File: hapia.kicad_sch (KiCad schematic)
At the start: 192 parts, among them J1 Micro_SD_Card, J10 USB_C_Receptacle_USB2.0_16P, J11 USB_A, J12 Micro_SD_Card, J2 SUB_placa_de_controle, J3 Conn_01x15_Pin, J4 ATX-20, J5 Conn_01x10, J6 Conn_01x04_Pin, J7 Conn_01x04_Pin, J8 Conn_01x04_Pin, J9 Conn_01x04_Pin, M1 Fan, M2 Fan, M3 Fan, Q1 NMOS, Q2 NMOS, Q3 NMOS, Q4 NMOS, SW1 SW_Push, SW2 SW_Push, U1 SRV05-4, U10 SRV05-4, U2 STM32F407VETx, U3 TMC2209-LA, U4 TMC2209-LA, U5 TPS54302, U6 TMC2209-LA, U7 TMC2209-LA, U8 MIC4427, U9 MIC4427, Y1 Crystal

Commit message: revisão 29072026 kicad 10
mais robusta, completa e mais perto de um lançamento funcional
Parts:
- removed C15, C18, C20, C21, C27, C31, C32, C33, C34, C36, C39, C40, C41, C46, C52, C58, C59, C61, C62, C64, C66, C71, C72, C74, C78, C79: 100nf, symbol Device:C
- removed C19, C35, C38, C63, C65: 1uf, symbol Device:C
- removed C23: 470µf, symbol Device:C_Polarized
- removed C26, C45, C47, C49, C73, C75: 10uf, symbol Device:C
- removed C28, C30, C56, C57: 22nf, symbol Device:C
- removed C29, C37, C43, C67, C69: 10nf, symbol Device:C
- removed C42, C44, C70: 4.7uf, symbol Device:C
- removed C48, C50, C76, C77: 100uf, symbol Device:C
- removed C51: 470uf, symbol Device:C
- removed C54: 100µf, symbol Device:C_Polarized
- removed C60: 1nf, symbol Device:C
- removed D1: SMF15A, Diode_SMD:D_SMF, symbol Diode:SMF15A
- removed D2: SMF33A, Diode_SMD:D_SMF, symbol Diode:SMF33A
- removed F1, F3, F4: Polyfuse, symbol Device:Polyfuse
- removed F2, F5: Fuse, symbol Device:Fuse
- removed FB1: FerriteBead, symbol Device:FerriteBead
- removed J1, J12: Micro_SD_Card, symbol Connector:Micro_SD_Card
- removed J11: USB_A, Connector_USB:USB_A_Molex_67643_Horizontal, symbol Connector:USB_A
- removed J2: SUB_placa_de_controle, Connector_PinHeader_2.54mm:PinHeader_1x10_P2.54mm_Vertical, symbol Connector_Generic:Conn_01x10
- removed J3: Conn_01x15_Pin, Connector_PinSocket_2.54mm:PinSocket_1x15_P2.54mm_Vertical, symbol Connector:Conn_01x15_Pin
- removed J4: ATX-20, Connector_Molex:Molex_Mini-Fit_Jr_5566-20A_2x10_P4.20mm_Vertical, symbol Connector:ATX-20
- removed J5: Conn_01x10, symbol Connector_Generic:Conn_01x10
- removed J6, J7, J8, J9: Conn_01x04_Pin, Connector_JST:JST_EH_B4B-EH-A_1x04_P2.50mm_Vertical, symbol Connector:Conn_01x04_Pin
- removed L1: 6.8uh, Inductor_SMD:L_Bourns_SRP1038C_10.0x10.0mm, symbol Device:L
- removed M1, M2, M3: Fan, symbol Motor:Fan
- removed Q1, Q2, Q3, Q4: NMOS, symbol Simulation_SPICE:NMOS
- removed R22, R23, R24, R25, R26, R27, R28, R29, R37, R38, R39, R40, R76, R77: 33r, symbol Device:R
- removed R34, R35, R36: 1k, symbol Device:R
- removed R41, R42, R43, R44, R53, R55, R56, R57, R58: 100k, symbol Device:R
- removed R45, R46, R59, R60: 20k, symbol Device:R
- removed R47, R48, R49, R50, R61, R62, R63, R64: 11r, symbol Device:R
- removed R51, R52: 10kΩ, symbol Device:R
- removed R54: 22k, symbol Device:R
- removed R65: 1Ωm, symbol Device:R
- removed R66, R67, R68, R73: 10k, symbol Device:R
- removed R69, R70: exrtusora, symbol Device:Heater
- removed R74: R, symbol Device:R
- removed TH1, TH2: 10k, symbol Device:Thermistor_NTC
- removed TP1, TP2, TP3, TP4, TP6, TP7, TP8, TP9: TestPoint, Connector_USB:USB_Micro-B_Amphenol_10104110_Horizontal, symbol Connector:TestPoint
- removed U1: SRV05-4, Package_TO_SOT_SMD:SOT-23-6, symbol Power_Protection:SRV05-4
- removed U3, U4, U6, U7: TMC2209-LA, Package_DFN_QFN:VQFN-28-1EP_5x5mm_P0.5mm_EP3.7x3.7mm_ThermalVias, symbol Driver_Motor:TMC2209-LA
- removed U5: TPS54302, Package_TO_SOT_SMD:SOT-23-6, symbol Regulator_Switching:TPS54302
- removed U8, U9: MIC4427, symbol Driver_FET:MIC4427
- added C14: 10µf, symbol Device:C
- added C95: 1µf, symbol Device:C
- added D5: SMF33A, Diode_SMD:D_SMF, symbol Diode:SMF33A
- added JP1: usb/atx, symbol Jumper:SolderJumper_3_Bridged12
- added R10, R16, R6, R7, R8, R9: 33Ω, symbol Device:R
- added R18: 10kΩ, symbol Device:R
- added unit 8 of RN1
- added unit 3 of RN3
- added unit 2 of RN3
- added unit 5 of RN3
- added unit 7 of RN3
- added unit 6 of RN3
- added unit 1 of RN3
- added unit 4 of RN3
- added RN4, RN5: 33Ω, Resistor_SMD:R_Array_Convex_4x0603, symbol Device:R_Pack04_Split
- added TP16: 3.3va, TestPoint:TestPoint_Pad_D1.0mm, symbol Connector:TestPoint
- added U1: AMS1117-3.3, Package_TO_SOT_SMD:SOT-223-3_TabPin2, symbol Regulator_Linear:AMS1117-3.3
- C1: value pf -> 22pf; footprint (none) -> Capacitor_SMD:C_0603_1608Metric_Pad1.08x0.95mm_HandSolder; jlc_pcb: (none) -> C561800; mpn (none) -> C0603C220J4GAC7867
- C10, C2, C3, C4, C5, C6, C7, C9: footprint (none) -> Capacitor_SMD:C_0603_1608Metric; jlc_pcb/lcsc_ID: (none) -> C346191; jlc_pcb: (none) -> C346191; mpn (none) -> CL10B104KB8NFNC
- C11: renamed from C13; value pf -> 22pf; footprint (none) -> Capacitor_SMD:C_0603_1608Metric_Pad1.08x0.95mm_HandSolder; jlc_pcb: (none) -> C561800; mpn (none) -> C0603C220J4GAC7867
- C12: renamed from C11; footprint (none) -> Capacitor_SMD:C_0603_1608Metric; jlc_pcb/lcsc_ID: (none) -> C346191; jlc_pcb: (none) -> C346191; mpn (none) -> CL10B104KB8NFNC
- C13: renamed from C12; value 10uf -> 10µf
- C15: renamed from C14; value 4.7uf -> 2.2µf
- C16: value 10uf -> 2.2µf
- C17: value 4.7uf -> 1µf
- C68: value 4.7uf -> 100nf; footprint (none) -> Capacitor_SMD:C_0603_1608Metric; jlc_pcb/lcsc_ID: (none) -> C346191; jlc_pcb: (none) -> C346191; mpn (none) -> CL10B104KB8NFNC
- C8: value 10uf -> 100nf; footprint (none) -> Capacitor_SMD:C_0603_1608Metric; jlc_pcb/lcsc_ID: (none) -> C346191; jlc_pcb: (none) -> C346191; mpn (none) -> CL10B104KB8NFNC
- R1, R2: value 10K -> 10KΩ
- R19: renamed from R75; value R -> 10kΩ
- R20: renamed from R71; value 5.1Ωk -> 5.1kΩ
- R21: renamed from R72; value 5.1Ωk -> 5.1kΩ
- R3, R4: value 4.7k -> 33Ω
- R5: value 33r -> 33Ω
- TP1: renamed from TP5; value TestPoint -> 3.3v; footprint Connector_USB:USB_Micro-B_Amphenol_10104110_Horizontal -> TestPoint:TestPoint_Pad_D1.0mm
- TP2: renamed from TP10; footprint Connector_USB:USB_Micro-B_Amphenol_10104110_Horizontal -> TestPoint:TestPoint_Pad_D1.0mm
- U2: value STM32F407VETx -> STM32F407VET6; jlc_pcb: (none) -> C28730; mpn (none) -> STM32F407VET6
- U3: renamed from U10; jlc_pcb: (none) -> ssss; mpn (none) -> ssss
- Y1: value Crystal -> 8mhz; footprint (none) -> Crystal:Crystal_SMD_5032-2Pin_5.0x3.2mm_HandSoldering; jlc_pcb: (none) -> C144380; mpn (none) -> ABM3-8.000MHZ-D2Y-T
- renumbered J10 to J1, R78 to R11, R30 to R12, R31 to R13, R32 to R14, R33 to R15, RN1 to RN2, RN2 to RN3
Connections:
- net PGND is gone; now on an unnamed net: C68.1
- net TMC_4vut is gone; now on net GND: C68.2
- net USB_D+ is gone; now on net USB_C_D+: RN3.9 (R8.2)
- net USB_D- is gone; now on net USB_C_D-: RN2.10 (R7.2)
- net +3.3V: now also JP1.3 (B); no longer C10.1, C12.1, C13.1, C16.1, C2.1, C3.1, C4.1, C5.1, C6.1, C7.1, C8.1, C9.1, FB2.2, R1.2, R2.2, R3.1, R4.1, SW1.2, SW2.2, U2.100 (VDD), U2.11 (VDD), U2.14 (NRST), U2.19 (VDD), U2.28 (VDD), U2.50 (VDD), U2.6 (VBAT), U2.75 (VDD), U2.94 (BOOT0)
- net Fan_1: now also R8.2
- net Fan_2: now also R4.2; no longer R5.2
- net GND: now also C14.2, C95.2, D5.2 (A2), U1.1 (GND)
- net SUB_2: now also RN3.14 (R3.2); no longer U2.91 (PB5)
- net SUB_3: now also RN3.13 (R4.2); no longer U2.92 (PB6)
- net SUB_4: now also RN3.12 (R5.2); no longer U2.93 (PB7)
- net SUB_5: now also RN3.11 (R6.2); no longer U2.95 (PB8)
- net SUB_6: now also RN3.10 (R7.2); no longer U2.96 (PB9)
- net SUB_SCL: now also RN3.16 (R1.2); no longer R4.2
- net SUB_SDA: now also RN3.15 (R2.2); no longer R3.2
- net USB_det_2.5v: now also R18.2
- net exrtusora: now also R6.2
- net gpi_PD14: now also R10.2
- net gpi_PD15: now also R9.2
- net hot_bed: now also R7.2
- net sd_cs: now also R5.2
- net at U2.25 (PA2): now also RN4.8 (R1.2)
- net at U2.26 (PA3): now also RN4.7 (R2.2)
- net at U2.36 (PB1): now also R7.1
- net at U2.35 (PB0): now also R6.1
- net at U2.73 (VCAP_2): now also C16.1; no longer C17.1
- net at R15.2, U2.24 (PA1): now also R16.1
- net at U2.22 (VDDA): now also FB2.1, C95.1, TP16.1; no longer TP1.1
- net at U2.29 (PA4): now also RN4.6 (R3.2)
- net at U2.30 (PA5): now also RN4.5 (R4.2)
- net at U2.31 (PA6): now also RN5.8 (R1.2)
- net at U2.32 (PA7): now also RN5.7 (R2.2)
- net at U2.33 (PC4): now also RN5.6 (R3.2)
- net at U2.34 (PC5): now also RN5.5 (R4.2)
- net at U2.37 (PB2): now also R8.1
- net at U2.38 (PE7): now also R4.1; no longer R5.1
- net NTC_MUX_out: now reaches U2.39 (PE8)
- net NTC_MUX_0: now reaches U2.40 (PE9)
- net NTC_MUX_1: now reaches U2.41 (PE10)
- net NTC_MUX_2: now reaches U2.42 (PE11)
- net at U2.63 (PC6): now also R9.1
- net at U2.64 (PC7): now also R10.1
- net at U2.77 (PA15): now also R5.1
- net at U2.89 (PB3): now also RN3.1 (R1.1)
- net at U2.90 (PB4): now also RN3.2 (R2.1)
- net at U2.97 (PE0): now also RN1.8 (R8.1)
- net at U2.98 (PE1): now also R3.1
- net 3.3v/A: no longer names the net of U2.21 (VREF+)
- net USB_det renamed +5Vusb
- net +5Vusb: now also C14.1, R18.1, U1.3 (VI)
- new net: RN3.3 (R3.1), U2.91 (PB5)
- new net: RN3.5 (R5.1), U2.93 (PB7)
- new net: RN3.4 (R4.1), U2.92 (PB6)
- new net: RN3.6 (R6.1), U2.95 (PB8)
- new net: RN3.7 (R7.1), U2.96 (PB9)
- new net +3.3Vbus: C17.1, D5.1 (A1), JP1.1 (A), U1.2 (VO)
- new net 3.3v/1: C10.1, C12.1, C13.1, C2.1, C3.1, C4.1, C5.1, C6.1, C7.1, C8.1, C9.1, FB2.2, JP1.2 (C), R1.2, R2.2, SW1.2, SW2.2, TP1.1, U2.100 (VDD), U2.11 (VDD), U2.14 (NRST), U2.19 (VDD), U2.28 (VDD), U2.50 (VDD), U2.6 (VBAT), U2.75 (VDD), U2.94 (BOOT0)
- new net SUB_led: RN1.9 (R8.2)
- new net TMC_DIR_3: RN4.1 (R1.1), RN4.3 (R3.1), RN5.1 (R1.1), RN5.3 (R3.1)
- new net TMC_step_3: RN4.2 (R2.1), RN4.4 (R4.1), RN5.2 (R2.1), RN5.4 (R4.1)
- new net TMC_uart: R16.2
- new net cont_sd: R3.2
- no-connect marks 76 -> 36
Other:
- note added: "3.3vbus = usb 3.3v = atx"
- note added: "by todio"
- note added: "ele ja vem com alimentaçao por usb"
- moved on the sheet: C1, C10, C11, C12, C13, C15, C2, C3, C4, C5, C6, C7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

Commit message: 10082026/B
nova revisão
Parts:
- removed C10, C12, C6, C68, C7, C8, C9: 100nf, Capacitor_SMD:C_0603_1608Metric, symbol Device:C
- removed C15: 2.2µf, symbol Device:C
- removed C95: 1µf, symbol Device:C
- removed R1, R2: 10KΩ, symbol Device:R
- added C29: 4.7µf, symbol Device:C
- added CN1, CN2: C_Network04, Resistor_SMD:R_Array_Convex_4x0603, symbol Device:C_Network04
- added D1: RED, symbol Device:LED_Small
- added F1: Fuse, symbol Device:Fuse
- added J18: Conn_ARM_JTAG_SWD_10, symbol Connector:Conn_ARM_JTAG_SWD_10
- added R1: 470Ω, symbol Device:R_Small
- added R22, R23: 33Ω, symbol Device:R
- added R42, R43: 10KΩ, symbol Device:R
- added TP12: TestPoint, TestPoint:TestPoint_Pad_D1.0mm, symbol Connector:TestPoint
- C16: value 2.2µf -> 4.7µf
- TP16: value 3.3va -> TestPoint
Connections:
- net +5Vusb: now also F1.2; no longer J1.A4 (VBUS), J1.A9 (VBUS), J1.B4 (VBUS), J1.B9 (VBUS), TP2.1, U3.2 (VN)
- net 3.3v/1: now also CN1.1 (common), CN1.2 (C1), CN1.3 (C2), CN1.4 (C3), CN2.2 (C1), CN2.3 (C2), CN2.4 (C3), R42.2, R43.2; no longer C2.1, C3.1, C4.1, C5.1, SW1.2, SW2.2, U2.14 (NRST), U2.94 (BOOT0)
- net GND: now also C29.2, CN1.5 (C4), CN1.6 (C3), CN1.7 (C2), CN1.8 (C1), CN2.5 (C4), CN2.6 (C3), CN2.7 (C2), CN2.8 (C1), J18.3 (GND), J18.5 (GND), J18.9 (GNDDetect), R1.1
- net at RN3.2 (R2.1): no longer U2.90 (PB4)
- net VDDA: now reaches FB2.1, U2.22 (VDDA)
- net VDDA: now also U2.21 (VREF+), CN2.1 (common); no longer TP16.1
- net at U2.49 (VCAP_1): now also C4.1, C29.1
- net at U2.72 (PA13): now also R23.1
- net at C16.1, U2.73 (VCAP_2): now also C5.1
- net at U2.76 (PA14): now also R22.1
- net at RN3.1 (R1.1): no longer U2.89 (PB3)
- net +3.3Vbus renamed +3.3Vdev
- net +3.3Vdev: now also J18.1 (VTref)
- new net: D1.2 (A), F1.1, J1.A4 (VBUS), J1.A9 (VBUS), J1.B4 (VBUS), J1.B9 (VBUS), TP2.1, U3.2 (VN)
- new net: D1.1 (K), R1.2
- new net SDW_SWCLK: J18.4 (SWCLK/TCK), R22.2
- new net SDW_SWDIO: J18.2 (SWDIO/TMS), R23.2
- new net STM_boot: C3.1, R43.1, SW2.2, TP12.1, U2.94 (BOOT0)
- new net STM_nrst: C2.1, R42.1, SW1.2, TP16.1, U2.14 (NRST)
- new net SWD_SWO: J18.6 (SWO/TDO), U2.89 (PB3)
- new net SWD/jtag_rst: J18.10 (~{RESET}), U2.90 (PB4)
- no-connect marks 36 -> 34
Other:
- note added: "3.3vbus = usb, 3.3v = atx"
- note added: "Q1"
- note added: "Q1: o pino "shield" ta em "nc" por que essa impresora vai ser um "slave"/device, com modificação funciona com pendrive."
- note added: "Q2"
- note added: "se o mcu não tiver ligando com usb possivelmente o problema e o jumper(o pino do meio) não ligado a o pino de cima o 3.3vdev ou fusivel queimado. se esse não for o defeito provavelmente e algum componente com defeito."
- note removed: "3.3vbus = usb 3.3v = atx"
- company: (none) -> ---
- title: (none) -> hapia placa base.
- moved on the sheet: C13, FB2, R20, R21, RN3A, RN3B

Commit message: 10082026/D
"erros bobos"
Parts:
- CN1, CN2: value C_Network04 -> 100nf
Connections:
- net at RN3.2 (R2.1): now also U2.48 (PB11)
- net at U2.47 (PB10): now also RN3.1 (R1.1)
- no-connect marks 34 -> 33
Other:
- moved on the sheet: RN3A, RN3B
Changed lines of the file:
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@@
 	)
 	(no_connect
-		(at 128.27 163.83)
-	)
-	(no_connect
 		(at 201.93 66.04)
 	)
@@
 	)
 	(no_connect
-		(at 128.27 166.37)
+		(at 154.94 165.735)
 	)
 	(no_connect
@@
 	(global_label "SUB_SCL"
 		(shape input)
-		(at 160.655 146.05 0)
+		(at 135.89 163.83 0)
 		(fields_autoplaced yes)
 		(effects
@@
 		)
 		(property "Intersheetrefs" "${INTERSHEET_REFS}"
-			(at 171.9254 146.05 0)
+			(at 147.1604 163.83 0)
 			(hide yes)
 			(show_name no)
@@
 	(global_label "SUB_SDA"
 		(shape input)
-		(at 160.655 148.59 0)
+		(at 135.89 166.37 0)
 		(fields_autoplaced yes)
 		(effects
@@
 		)
 		(property "Intersheetrefs" "${INTERSHEET_REFS}"
-			(at 171.9859 148.59 0)
+			(at 147.2209 166.37 0)
 			(hide yes)
 			(show_name no)
@@
 	(symbol
 		(lib_id "Device:R_Pack08_Split")
-		(at 156.845 148.59 270)
+		(at 132.08 166.37 270)
 		(unit 2)
 		(body_style 1)
@@
 		(dnp no)
 		(property "Reference" "RN3"
-			(at 174.371 148.59 90)
+			(at 149.606 166.37 90)
 			(show_name no)
 			(do_not_autoplace no)
@@
 		)
 		(property "Value" "33Ω"
-			(at 156.845 148.59 90)
+			(at 132.08 166.37 90)
 			(show_name no)
 			(do_not_autoplace no)
@@
 		)
 		(property "Footprint" "Resistor_SMD:R_Array_Convex_8x0602"
-			(at 156.845 146.558 90)
+			(at 132.08 164.338 90)
 			(hide yes)
 			(show_name no)
@@
 		)
 		(property "Datasheet" ""
-			(at 156.845 148.59 0)
+			(at 132.08 166.37 0)
 			(hide yes)
 			(show_name no)
@@
 		)
 		(property "Description" "8 resistor network, parallel topology, split"
-			(at 156.845 148.59 0)
+			(at 132.08 166.37 0)
 			(hide yes)
 			(show_name no)
@@
 		)
 		(property "jlc_pcb/lcsc_ID:" ""
-			(at 156.845 148.59 0)
+			(at 132.08 166.37 0)
 			(hide yes)
 			(show_name no)
@@
 		)
 		(property "mpn" ""
-			(at 156.845 148.59 0)
+			(at 132.08 166.37 0)
 			(hide yes)
 			(show_name no)
@@
 			)
 		)
-		(property "Value" "C_Network04"
+		(property "Value" "100nf"
 			(at 26.2255 171.45 90)
 			(show_name no)
@@
 			)
 		)
-		(property "Value" "C_Network04"
+		(property "Value" "100nf"
 			(at 26.2255 149.86 90)
 			(show_name no)
@@
 	(symbol
 		(lib_id "Device:R_Pack08_Split")
-		(at 156.845 146.05 270)
+		(at 132.08 163.83 270)
 		(unit 1)
 		(body_style 1)
@@
 		(dnp no)
 		(property "Reference" "RN3"
-			(at 174.371 146.304 90)
+			(at 149.606 164.084 90)
 			(show_name no)
 			(do_not_autoplace no)
@@
 		)
 		(property "Value" "33Ω"
-			(at 156.845 146.05 90)
+			(at 132.08 163.83 90)
 			(show_name no)
 			(do_not_autoplace no)
@@
 		)
 		(property "Footprint" "Resistor_SMD:R_Array_Convex_8x0602"
-			(at 156.845 144.018 90)
+			(at 132.08 161.798 90)
 			(hide yes)
 			(show_name no)
@@
 		)
 		(property "Datasheet" ""
-			(at 156.845 146.05 0)
+			(at 132.08 163.83 0)
 			(hide yes)
 			(show_name no)
@@
 		)
 		(property "Description" "8 resistor network, parallel topology, split"
-			(at 156.845 146.05 0)
+			(at 132.08 163.83 0)
 			(hide yes)
 			(show_name no)
@@
 		)
 		(property "jlc_pcb/lcsc_ID:" ""
-			(at 156.845 146.05 0)
+			(at 132.08 163.83 0)
 			(hide yes)
 			(show_name no)
@@
 		)
 		(property "mpn" ""
-			(at 156.845 146.05 0)
+			(at 132.08 163.83 0)
 			(hide yes)
 			(show_name no)

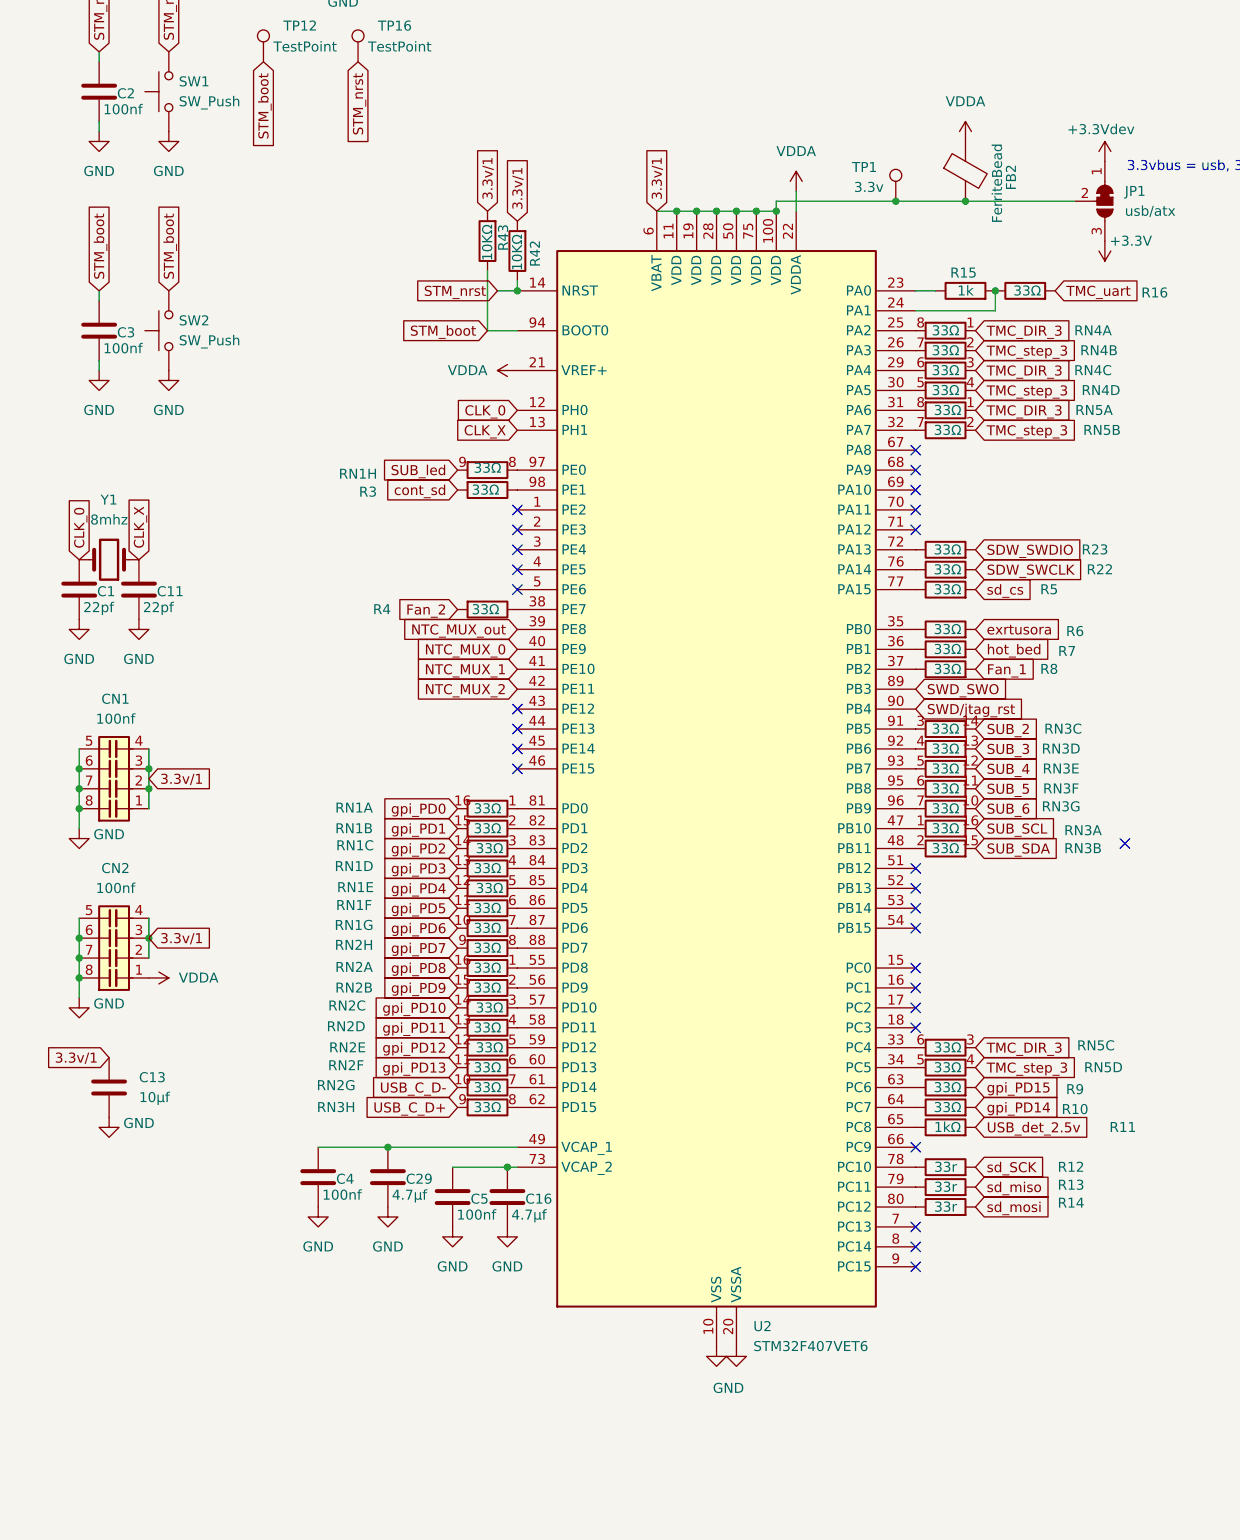
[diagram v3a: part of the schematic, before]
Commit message: 17082026/E
modulo FRAM e Melhoria no esquemático
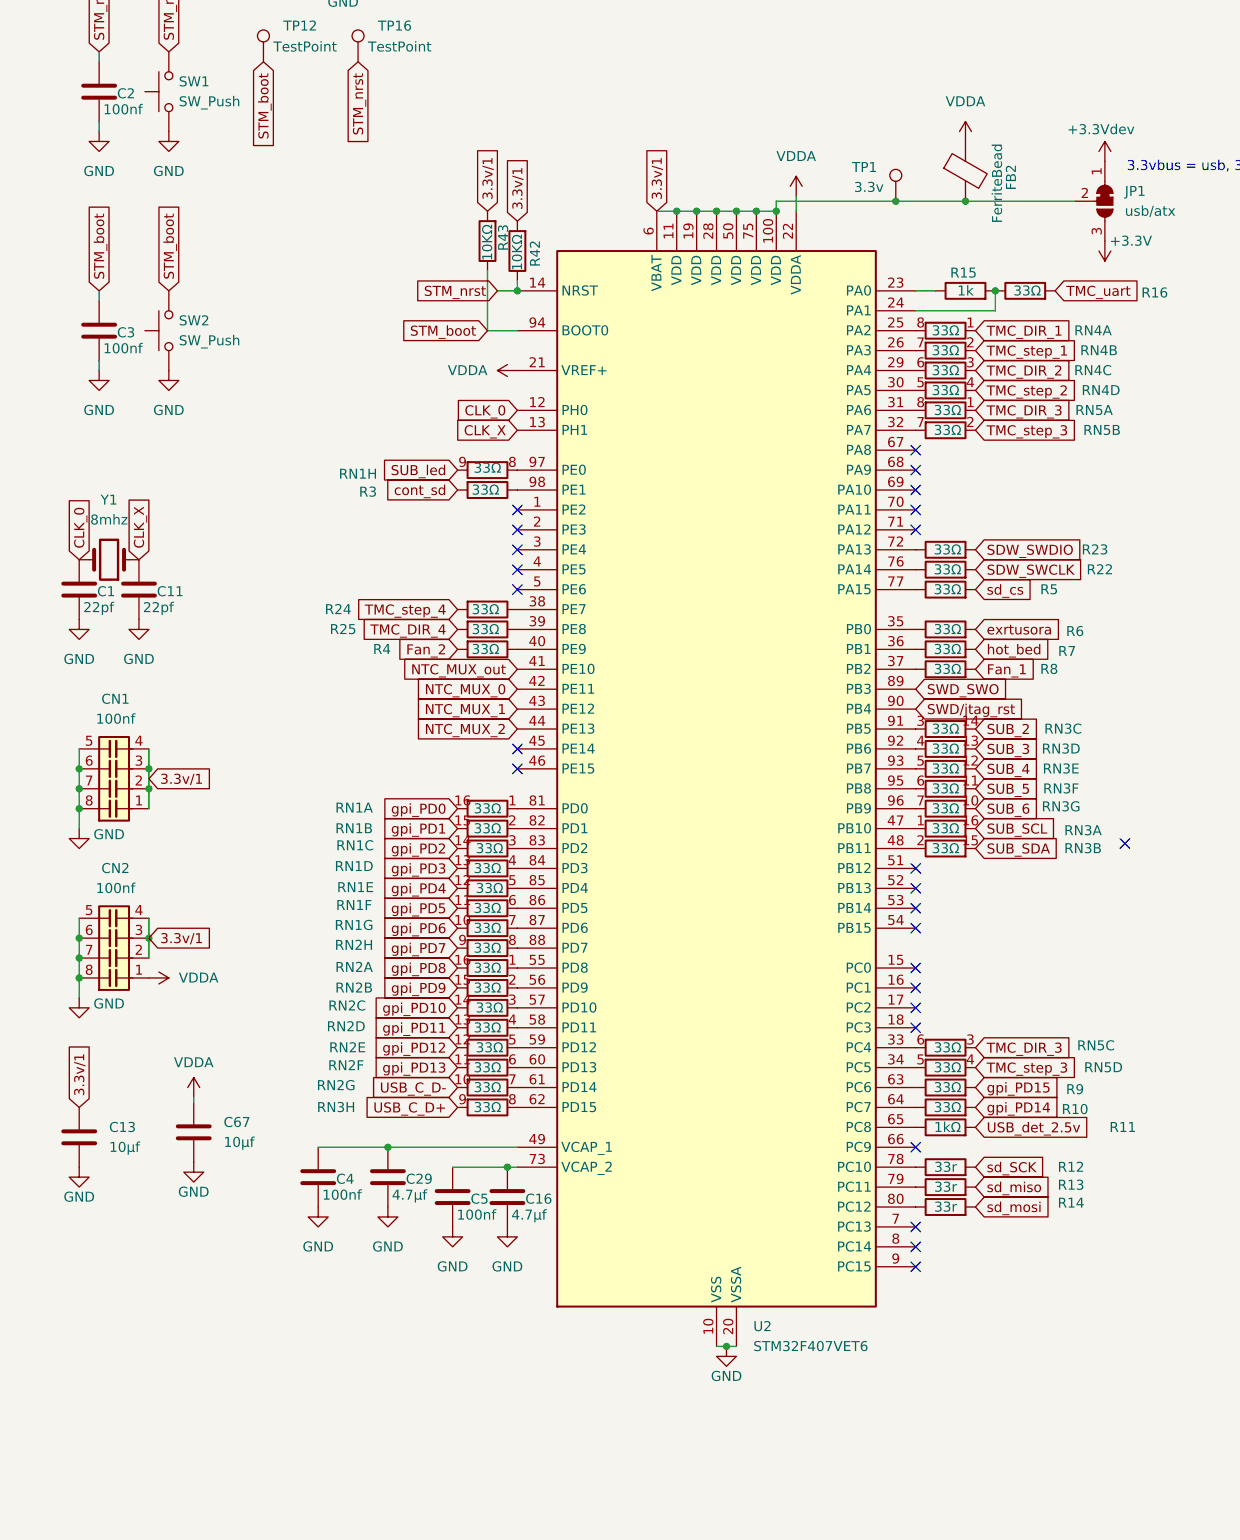
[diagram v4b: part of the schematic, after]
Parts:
- added C67: 10µf, symbol Device:C
- added R24, R25: 33Ω, symbol Device:R
- C17: footprint (none) -> Capacitor_SMD:C_0805_2012Metric_Pad1.18x1.45mm_HandSolder; jlc_pcb: (none) -> C28323
- CN1, CN2: footprint Resistor_SMD:R_Array_Convex_4x0603 -> Capacitor_SMD:C_0603_1608Metric; jlc_pcb: C576646 -> C346191
- JP1: footprint (none) -> Jumper:SolderJumper-3_P1.3mm_Bridged2Bar12_RoundedPad1.0x1.5mm
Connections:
- net GND: now also C67.2
- net NTC_MUX_0: now also U2.42 (PE11); no longer U2.40 (PE9)
- net NTC_MUX_1: now also U2.43 (PE12); no longer U2.41 (PE10)
- net NTC_MUX_2: now also U2.44 (PE13); no longer U2.42 (PE11)
- net NTC_MUX_out: now also U2.41 (PE10); no longer U2.39 (PE8)
- net TMC_DIR_3: no longer RN4.1 (R1.1), RN4.3 (R3.1)
- net TMC_step_3: no longer RN4.2 (R2.1), RN4.4 (R4.1)
- net VDDA: now also C67.1
- net at R4.1: now also U2.40 (PE9); no longer U2.38 (PE7)
- new net: R24.1, U2.38 (PE7)
- new net: R25.1, U2.39 (PE8)
- new net TMC_DIR_1: RN4.1 (R1.1)
- new net TMC_DIR_2: RN4.3 (R3.1)
- new net TMC_DIR_4: R25.2
- new net TMC_step_1: RN4.2 (R2.1)
- new net TMC_step_2: RN4.4 (R4.1)
- new net TMC_step_4: R24.2
- no-connect marks 33 -> 31
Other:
- moved on the sheet: C13, R4
